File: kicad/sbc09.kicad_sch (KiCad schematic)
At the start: 78 parts, among them J1 Conn_01x04_Male, J2 Conn_01x06_Male, J3 Conn_01x06_Male, J4 Conn_01x06_Male, J5 Conn_02x05_Odd_Even, J6 Conn_02x25_Odd_Even, Q1 2N7000, SW1 SW_Push, U1 74HCT245, U10 74LS670, U11 74LS670, U12 AS6C4008-55PCN, U13 SST39SF040-DIP, U14 SST39SF040-DIP, U15 XR68C681CJ, U16 MAX232, U17 GAL16V8, U2 74HCT245, U3 74HCT245, U4 MC6809E, U5 74HCT125, U6 ATF22V10C, U7 ATF22V10C, U8 74LS670, U9 74LS670, X1 8MHz, X2 3.6864MHz

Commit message: KiCAD - tidy up schematic
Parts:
- removed JP15: Jumper_3_Bridged12, Connector_PinHeader_2.54mm:PinHeader_1x03_P2.54mm_Vertical, symbol Jumper:Jumper_3_Bridged12
- added C17: 100n, Capacitor_THT:C_Disc_D4.7mm_W2.5mm_P5.00mm, symbol Device:C
- renumbered C17 to C24, JP16 to JP15
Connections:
- net 16KMODE: now also U7.3 (I1); no longer U7.2 (I0)
- net CLKX4: now also U5.12
- net E: now also U7.1 (OD/CLK)
- net GND: now also C17.2
- net Q: no longer U5.12
- net QA19: now also U7.4 (I2); no longer U7.3 (I1)
- net QA20: now also U7.5 (I3); no longer U7.4 (I2)
- net QA21: now also U7.6 (I4); no longer U7.5 (I3)
- net VCC: now also C17.1
- net nCSIO: now also U7.7 (I5); no longer U7.6 (I4)
- net nCSIOEXT: now also J6.29 (Pin_29)
- net nCSIOINT: now also U6.9 (I7), U7.8 (I6); no longer U6.15 (A0/O3), U7.7 (I5)
- net nENMMU: now also U7.2 (I0); no longer U7.1 (OD/CLK)
- net QBus renamed CLKX4Bus
- net SPARE: no longer names the net of U7.16 (A1/O2)
- no-connect marks 27 -> 25
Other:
- moved on the sheet: C10, C11, C12, C13, C14, C15, C16, C24, C9, J1, JP1, JP2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

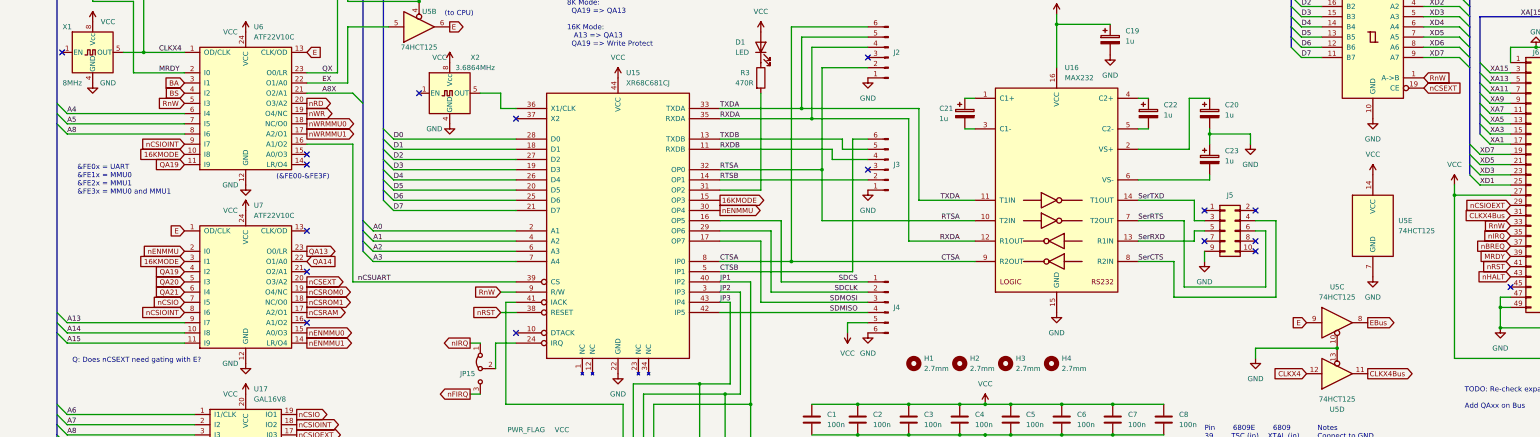
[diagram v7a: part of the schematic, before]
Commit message: Changes to support remote bus mastering
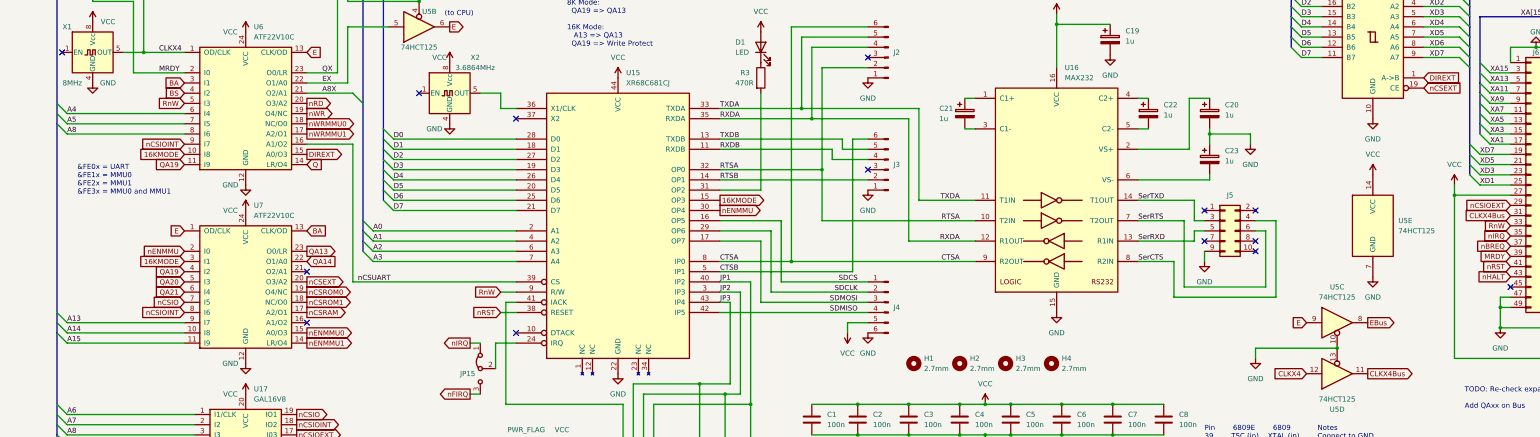
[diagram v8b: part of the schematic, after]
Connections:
- net BA: now also U7.13 (CLK/OD)
- net Q: now also U6.14 (LR/O4)
- net RnW: no longer U1.1 (A->B)
- net DIREXT: now reaches U6.15 (A0/O3)
- net DIREXT: now also U1.1 (A->B)
- no-connect marks 25 -> 22
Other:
- note removed: "(&FE00-&FE3F)"
- note removed: "Q: Does nCSEXT need gating with E?"
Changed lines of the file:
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@@
   (no_connect (at 74.93 269.24))
   (no_connect (at 120.65 270.51))
-  (no_connect (at 77.47 189.23))
   (no_connect (at 74.93 266.7))
   (no_connect (at 377.19 219.71))
@@
   (no_connect (at 129.54 231.14))
   (no_connect (at 129.54 177.8))
-  (no_connect (at 77.47 205.74))
   (no_connect (at 74.93 261.62))
   (no_connect (at 105.41 171.45))
   (no_connect (at 217.17 162.56))
-  (no_connect (at 77.47 186.69))
   (no_connect (at 389.89 214.63))
   (no_connect (at 16.51 161.29))
@@
     (effects (font (size 1.27 1.27)) (justify left bottom))
   )
-  (text "Q: Does nCSEXT need gating with E?" (at 19.05 238.76 0)
-    (effects (font (size 1.27 1.27)) (justify left bottom))
-  )
   (text "6809E: Open\n6809: Closed\n" (at 27.94 125.73 0)
     (effects (font (size 1.27 1.27)) (justify left bottom))
@@
     (effects (font (size 1.27 1.27)) (justify left bottom))
   )
-  (text "(&FE00-&FE3F)" (at 69.85 193.04 0)
-    (effects (font (size 1.27 1.27)) (justify left bottom))
-  )
   (text "(from bus)" (at 52.07 128.27 0)
     (effects (font (size 1.27 1.27)) (justify left bottom))
@@
     )
   )
-  (global_label "RnW" (shape input) (at 355.6 167.64 0) (fields_autoplaced)
+  (global_label "DIREXT" (shape input) (at 355.6 167.64 0) (fields_autoplaced)
     (effects (font (size 1.27 1.27)) (justify left))
-    (property "Intersheet References" "${INTERSHEET_REFS}" (id 0) (at 361.8836 167.5606 0)
+    (property "Intersheet References" "${INTERSHEET_REFS}" (id 0) (at 364.4841 167.5606 0)
       (effects (font (size 1.27 1.27)) (justify left) hide)
     )
@@
     )
   )
+  (global_label "Q" (shape input) (at 77.47 189.23 0) (fields_autoplaced)
+    (effects (font (size 1.27 1.27)) (justify left))
+    (property "Intersheet References" "${INTERSHEET_REFS}" (id 0) (at 81.2136 189.1506 0)
+      (effects (font (size 1.27 1.27)) (justify left) hide)
+    )
+  )
   (global_label "AVMA_MRDY" (shape bidirectional) (at 98.425 86.36 0) (fields_autoplaced)
     (effects (font (size 1.27 1.27)) (justify left))
@@
     )
   )
+  (global_label "BA" (shape input) (at 77.47 205.74 0) (fields_autoplaced)
+    (effects (font (size 1.27 1.27)) (justify left))
+    (property "Intersheet References" "${INTERSHEET_REFS}" (id 0) (at 82.2417 205.6606 0)
+      (effects (font (size 1.27 1.27)) (justify left) hide)
+    )
+  )
   (global_label "nCSROM1" (shape output) (at 77.47 223.52 0) (fields_autoplaced)
     (effects (font (size 1.27 1.27)) (justify left))
@@
   (global_label "E" (shape input) (at 46.99 205.74 180) (fields_autoplaced)
     (effects (font (size 1.27 1.27)) (justify right))
-    (property "Intersheet References" "${INTERSHEET_REFS}" (id 0) (at 43.4279 205.8194 0)
+    (property "Intersheet References" "${INTERSHEET_REFS}" (id 0) (at 43.4279 205.6606 0)
       (effects (font (size 1.27 1.27)) (justify right) hide)
     )
@@
     )
   )
+  (global_label "DIREXT" (shape output) (at 77.47 186.69 0) (fields_autoplaced)
+    (effects (font (size 1.27 1.27)) (justify left))
+    (property "Intersheet References" "${INTERSHEET_REFS}" (id 0) (at 86.3541 186.6106 0)
+      (effects (font (size 1.27 1.27)) (justify left) hide)
+    )
+  )
